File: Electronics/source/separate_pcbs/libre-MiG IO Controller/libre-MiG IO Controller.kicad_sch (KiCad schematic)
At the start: 30 parts, among them J10 Conn_01x03, J11 Conn_01x08, J12 Conn_01x08, J13 Conn_01x05, J14 Conn_01x03, J15 Conn_01x06, J8 Conn_01x03, J9 Conn_01x03, U2 TCA9535PWR, U3 TCA9535PWR, U6 MAX11615EEE

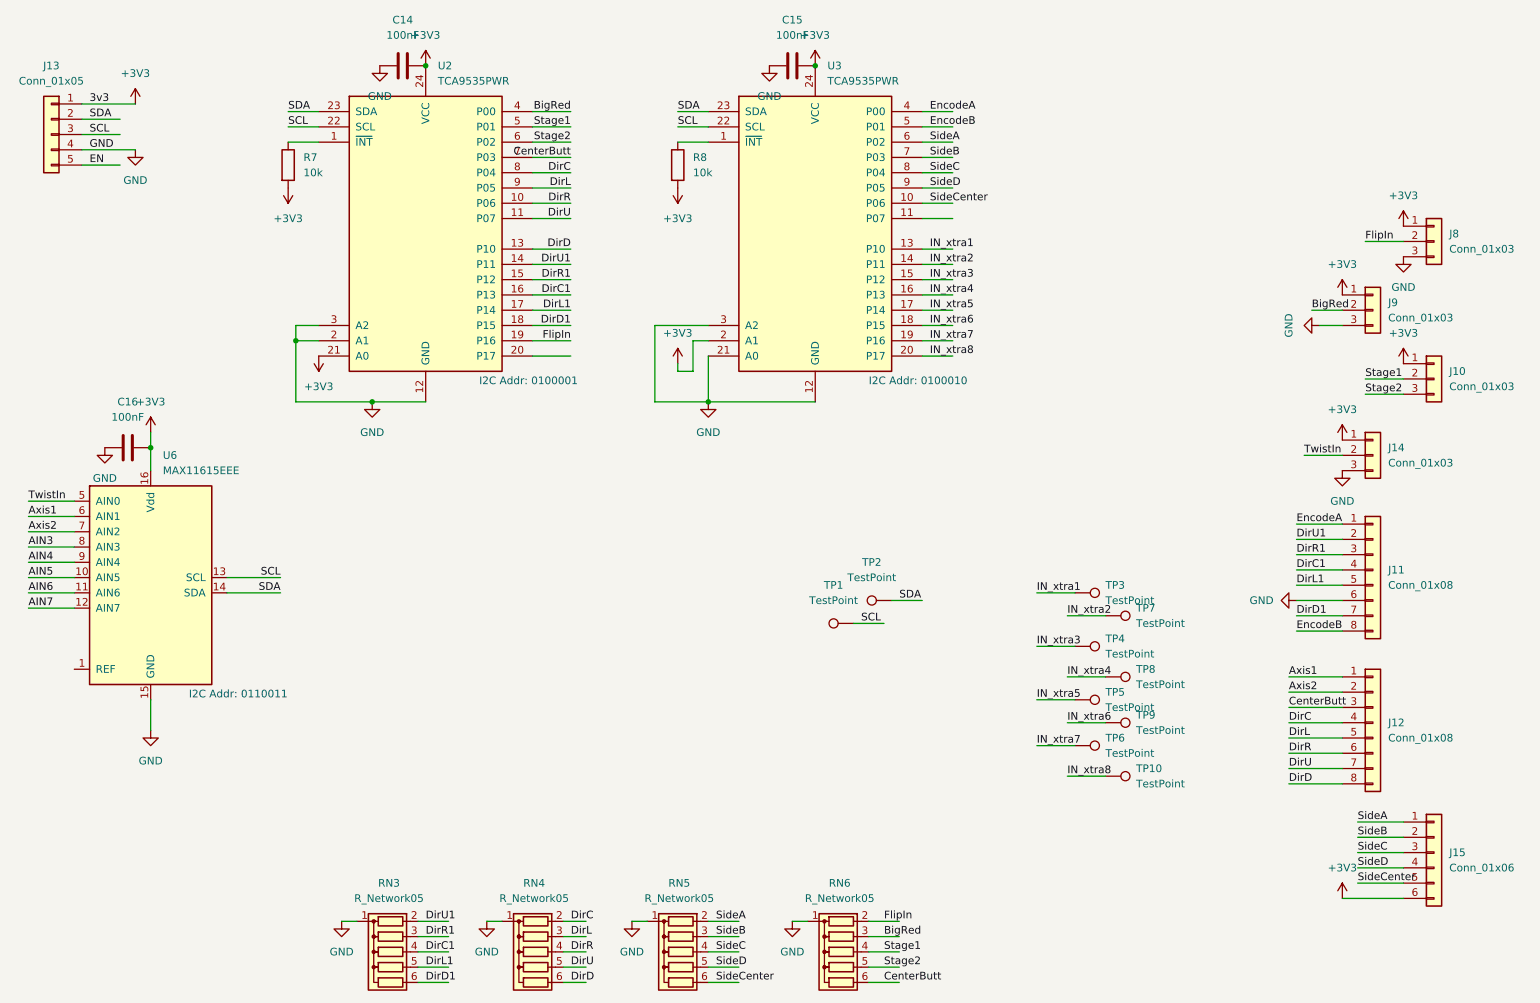
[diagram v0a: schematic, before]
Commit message: started layout and finished board shapes
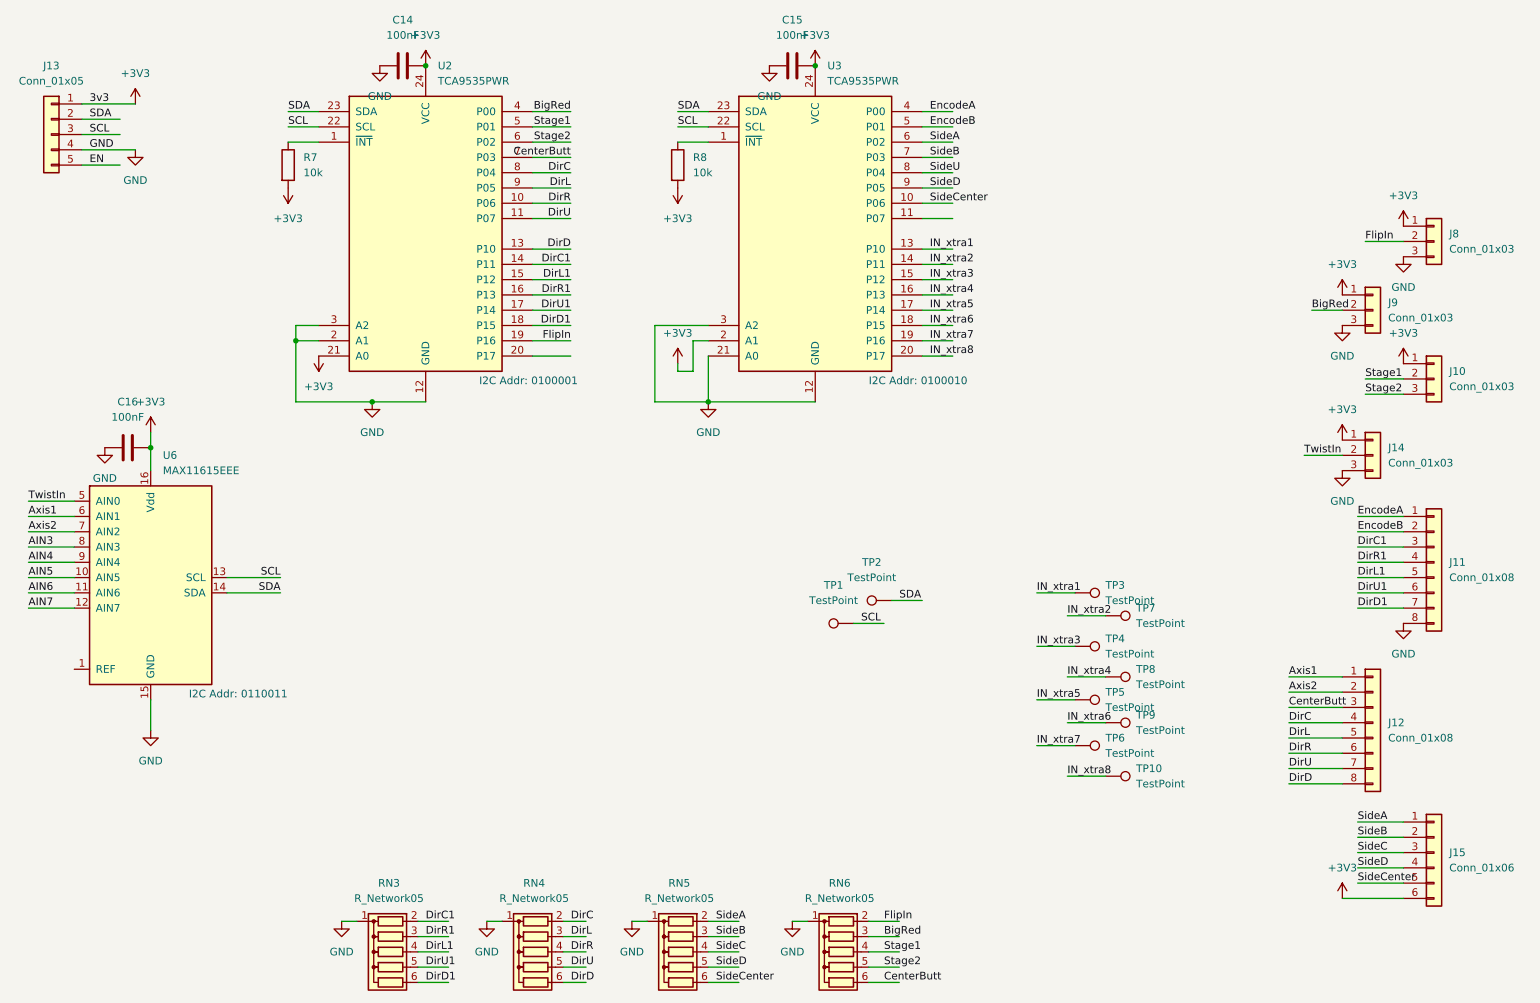
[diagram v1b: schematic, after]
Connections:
- net DirC1: now also J11.3 (Pin_3), RN3.2 (R1), U2.14 (P11); no longer J11.4 (Pin_4), RN3.4 (R3), U2.16 (P13)
- net DirL1: now also RN3.4 (R3), U2.15 (P12); no longer RN3.5 (R4), U2.17 (P14)
- net DirR1: now also J11.4 (Pin_4), U2.16 (P13); no longer J11.3 (Pin_3), U2.15 (P12)
- net DirU1: now also J11.6 (Pin_6), RN3.5 (R4), U2.17 (P14); no longer J11.2 (Pin_2), RN3.2 (R1), U2.14 (P11)
- net EncodeB: now also J11.2 (Pin_2); no longer J11.8 (Pin_8)
- net GND: now also J11.8 (Pin_8); no longer J11.6 (Pin_6)
- net SideC: no longer U3.8 (P04)
- new net SideU: U3.8 (P04)
